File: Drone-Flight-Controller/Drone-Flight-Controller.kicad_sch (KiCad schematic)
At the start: 45 parts, among them J1 Screw_Terminal_01x02, J10 TestPoint, J11 TestPoint, J12 TestPoint, J2 Raspberry_Pi_4, J3 TestPoint, J4 TestPoint, J5 TestPoint, J6 TestPoint, J7 TestPoint, J8 TestPoint, J9 TestPoint, SW1 SW_Omron_B3FS, U1 LMR51430, U2 ADC101C021CIMK, U3 MPU-9150, U4 BMP280, U5 PCA9531PW

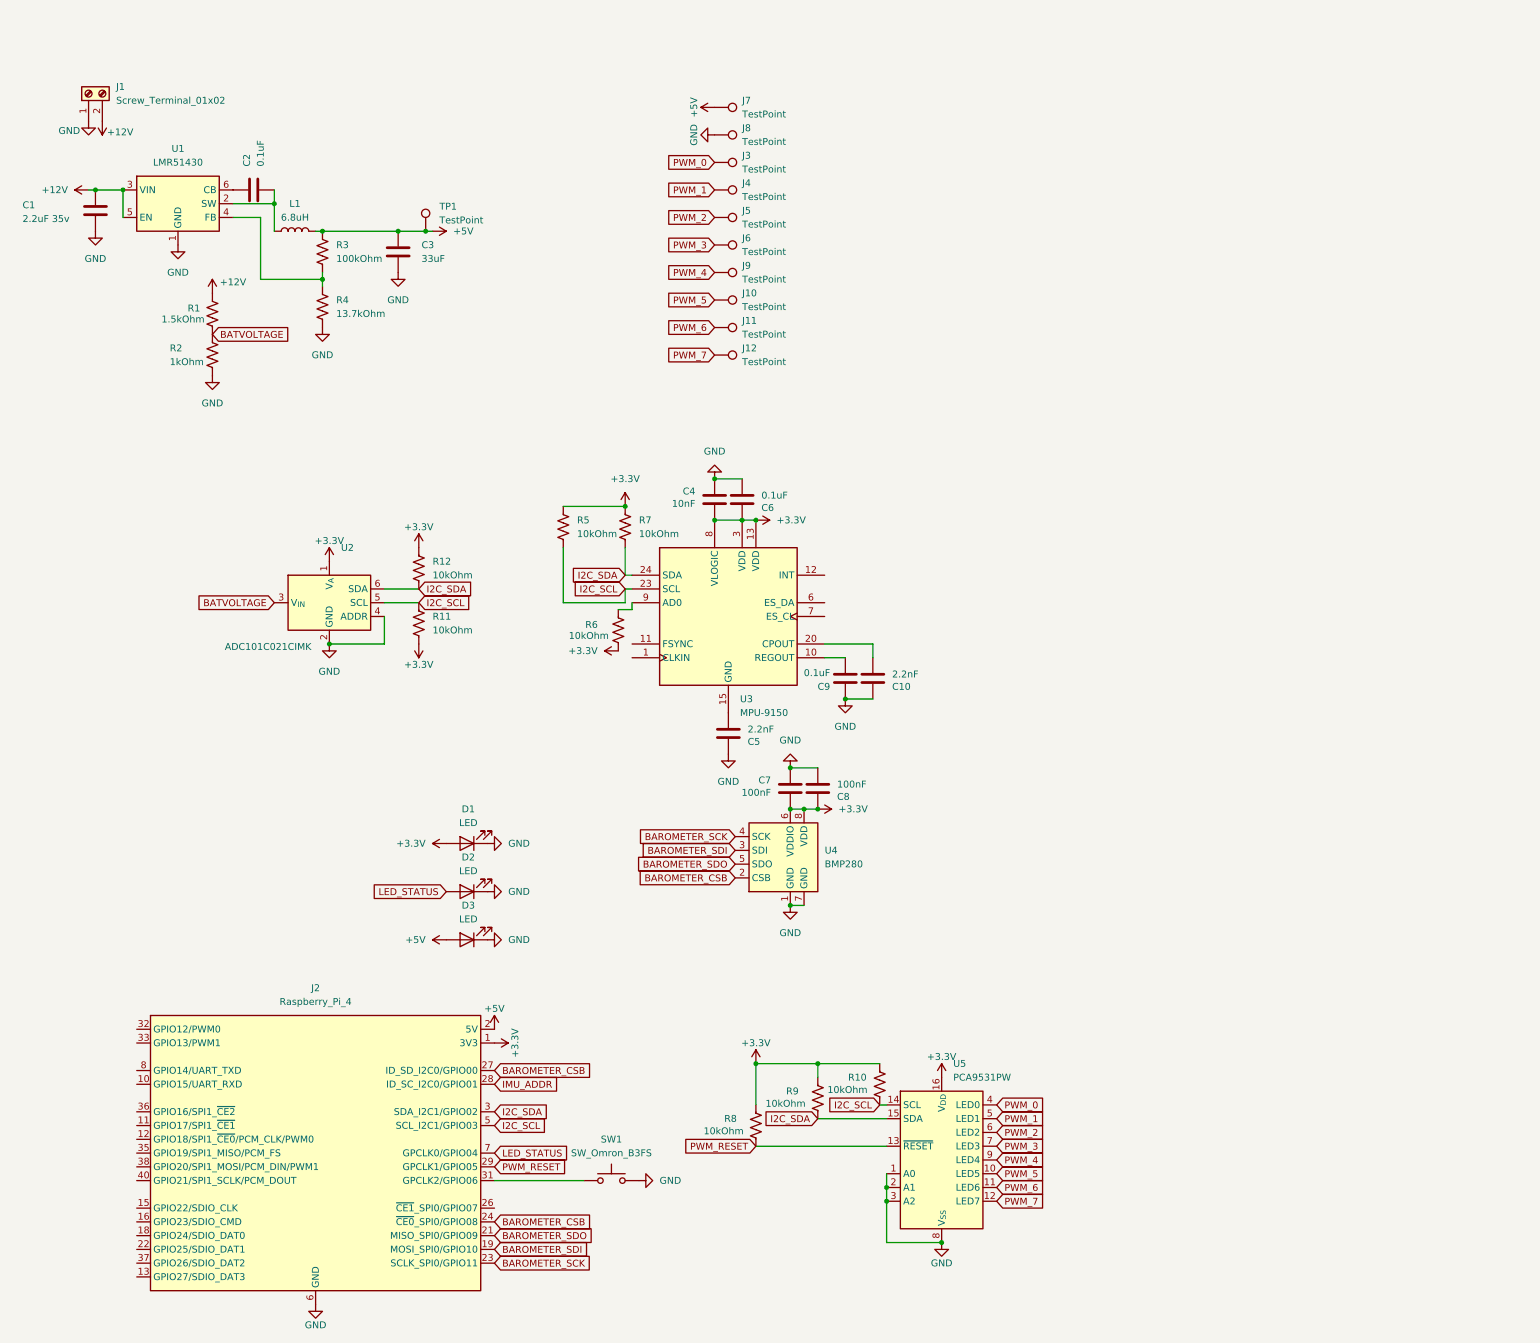
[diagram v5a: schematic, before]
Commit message: add a fuse
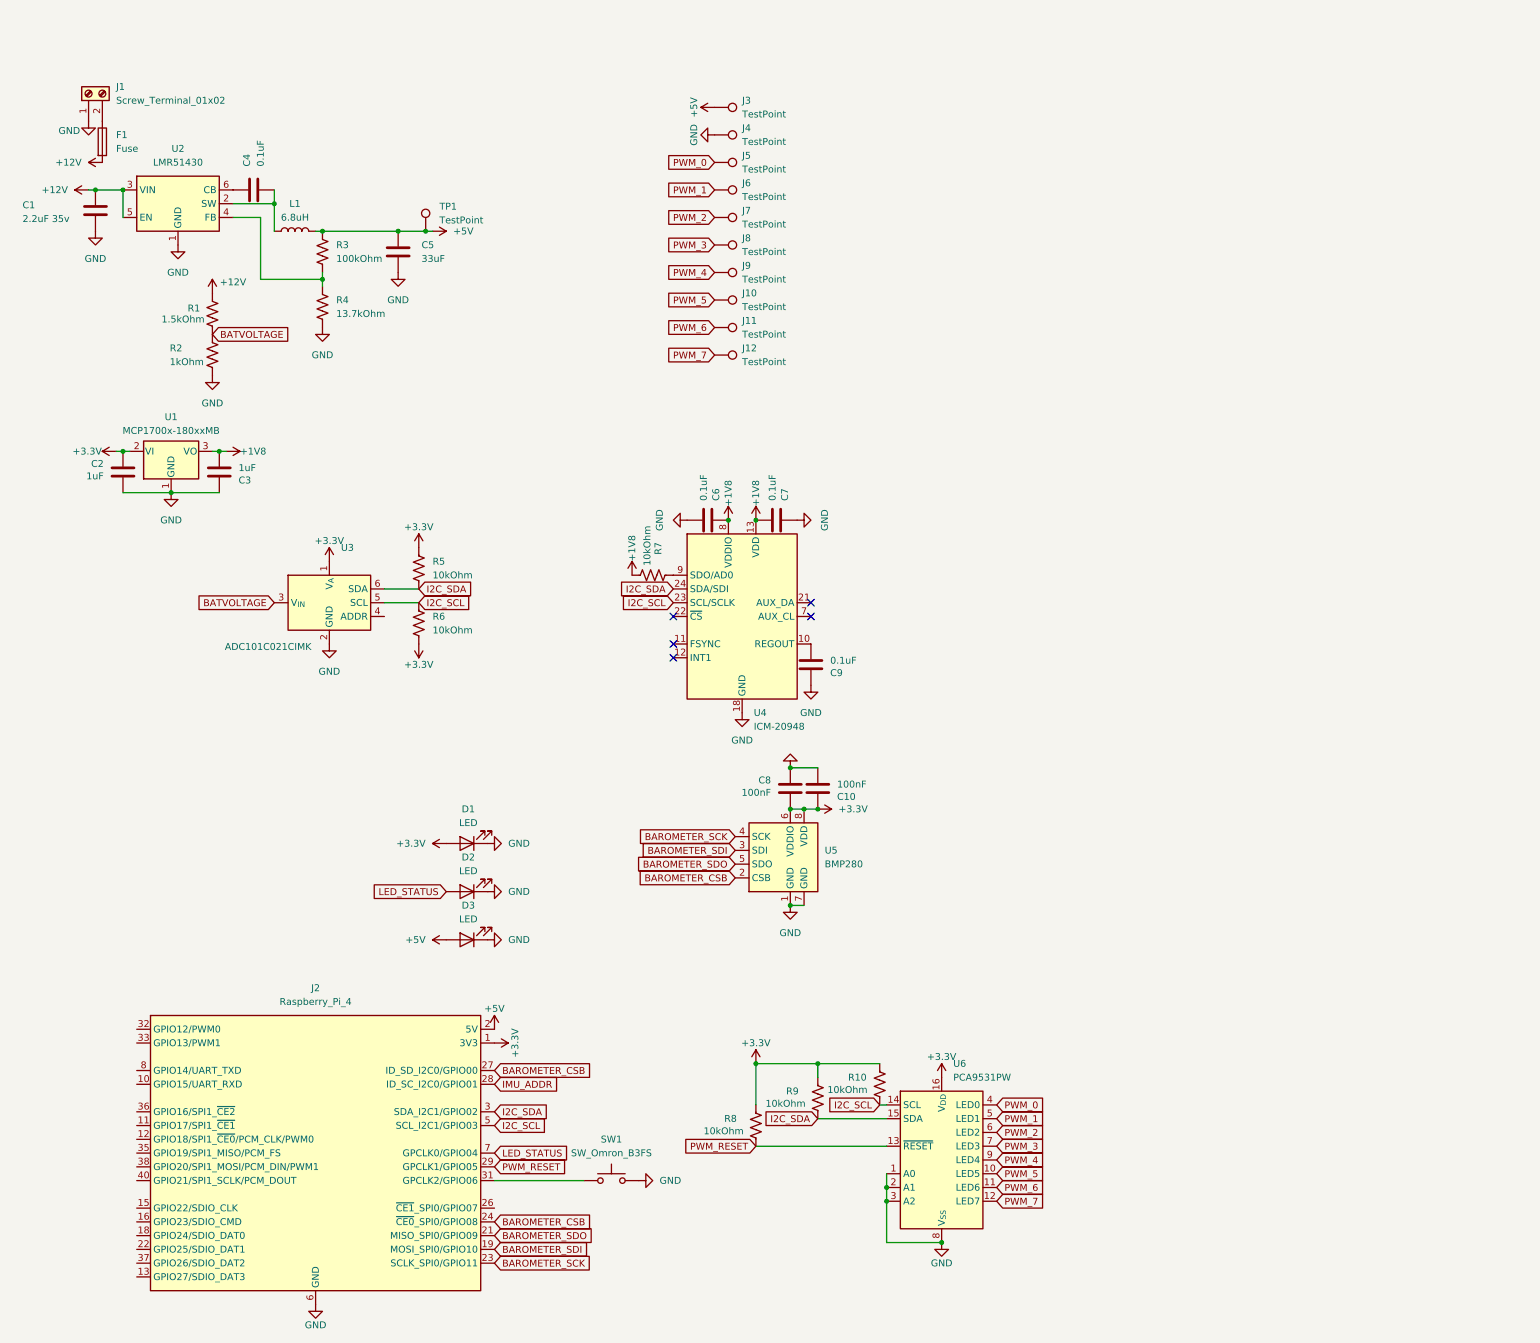
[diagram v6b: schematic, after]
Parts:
- removed C10, C5: 2.2nF, Capacitor_SMD:C_0402_1005Metric, symbol Device:C
- removed C4: 10nF, Capacitor_SMD:C_0402_1005Metric, symbol Device:C
- removed R5, R6: 10kOhm, Resistor_SMD:R_0402_1005Metric, symbol Device:R_US
- removed U3: MPU-9150, Sensor_Motion:InvenSense_QFN-24_4x4mm_P0.5mm, symbol Sensor_Motion:MPU-9150
- added C2, C3: 1uF, Capacitor_SMD:C_0402_1005Metric, symbol Device:C
- added C7: 0.1uF, Capacitor_SMD:C_0402_1005Metric, symbol Device:C
- added F1: Fuse, Fuse:Fuse_1206_3216Metric, symbol Device:Fuse
- added U1: MCP1700x-180xxMB, Package_TO_SOT_SMD:SOT-89-3, symbol Regulator_Linear:MCP1700x-180xxMB
- added U4: ICM-20948, Sensor_Motion:InvenSense_QFN-24_3x3mm_P0.4mm, symbol Sensor_Motion:ICM-20948
- renumbered C8 to C10, C2 to C4, C3 to C5, C7 to C8, J7 to J3, J8 to J4, J3 to J5, J4 to J6, J5 to J7, J6 to J8, R12 to R5, R11 to R6, U1 to U2, U2 to U3, U4 to U5, U5 to U6
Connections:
- net +12V: now also F1.2; no longer J1.2 (Pin_2)
- net +3.3V: now also C2.2, U1.2 (VI); no longer C6.2, R7.1
- net GND: now also C9.2, C2.1, C3.2, C7.2, U1.1 (GND), U4.18 (GND), U4.20 (GND); no longer C9.1, U3.4 (ADDR)
- net I2C_SCL: now also U4.23 (SCL/SCLK)
- net I2C_SDA: now also U4.24 (SDA/SDI); no longer R7.2
- new net: C9.1, U4.10 (REGOUT)
- new net: R7.1, U4.9 (SDO/AD0)
- new net: F1.1, J1.2 (Pin_2)
- new net +1V8: C3.1, C6.2, C7.1, R7.2, U1.3 (VO), U4.13 (VDD), U4.8 (VDDIO)
- no-connect marks 0 -> 5

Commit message: added imu level shifter
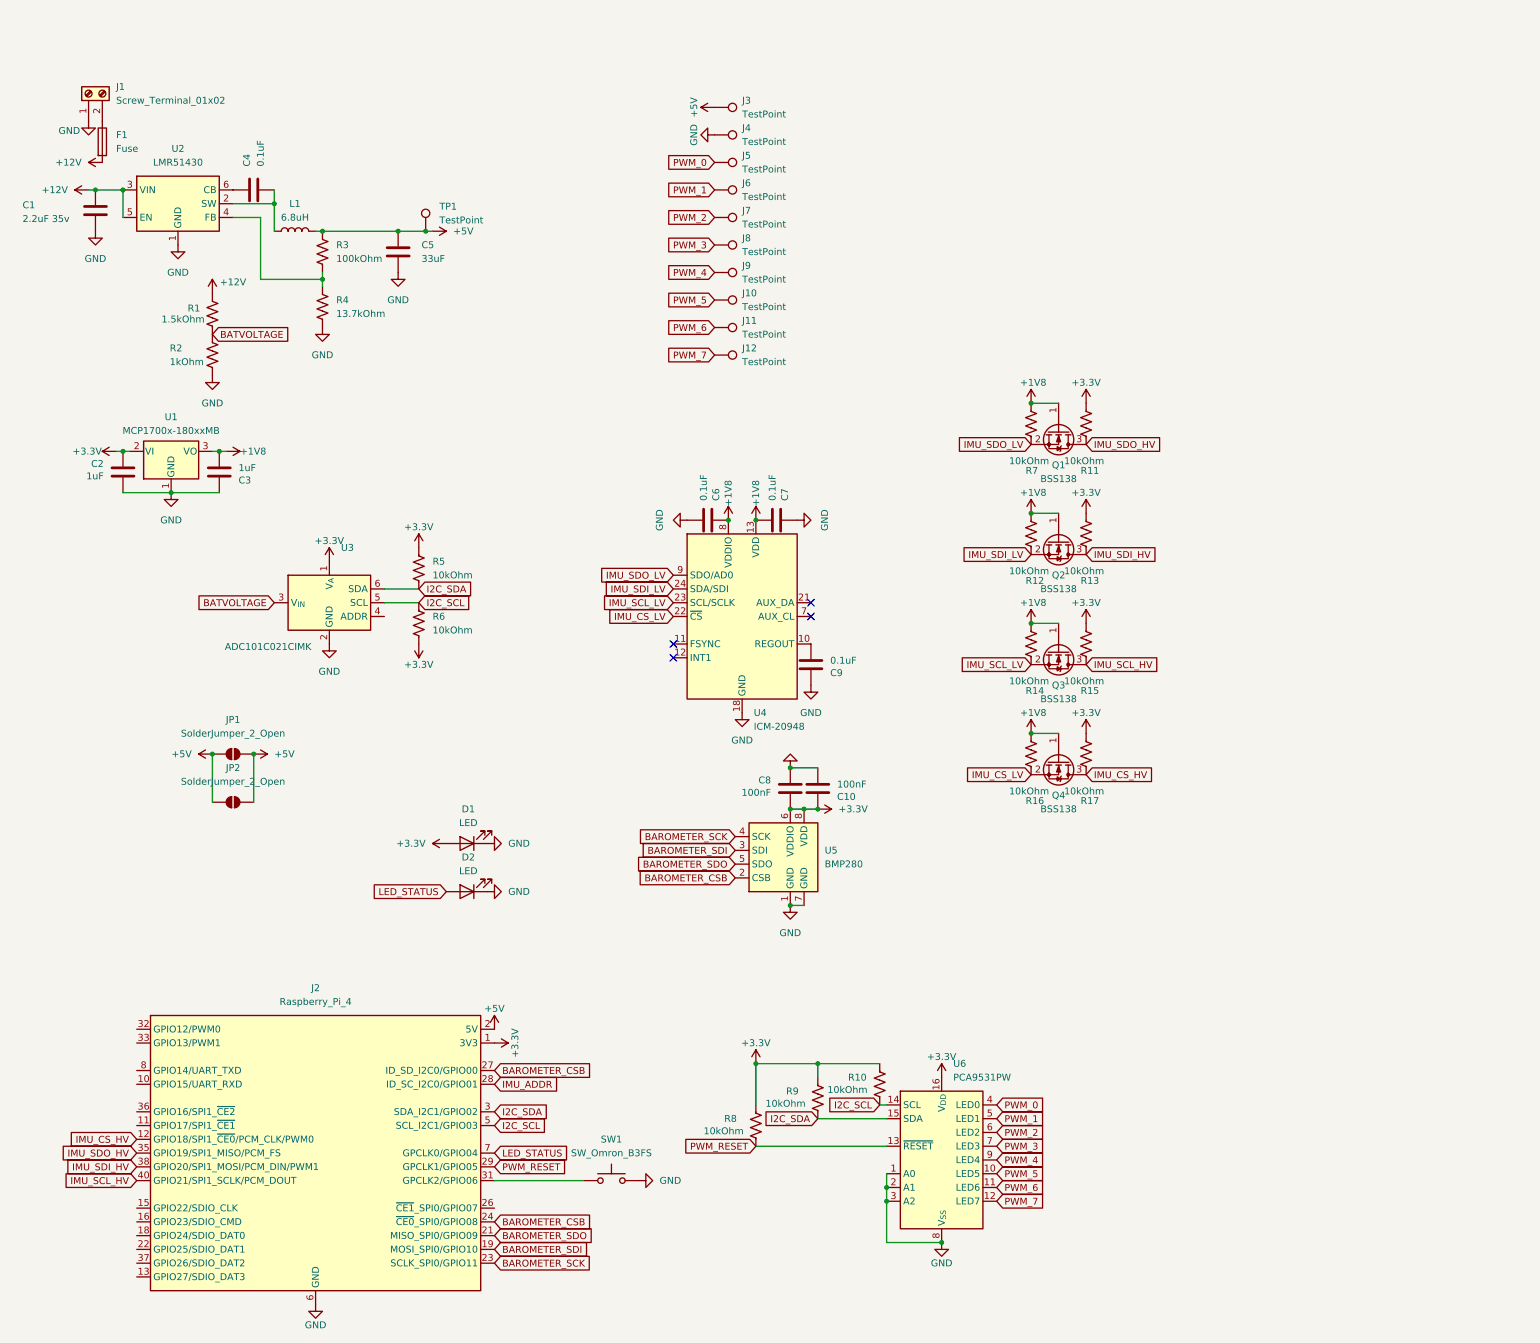
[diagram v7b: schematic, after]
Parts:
- removed D3: LED, LED_SMD:LED_0402_1005Metric, symbol Device:LED
- added JP1, JP2: SolderJumper_2_Open, Jumper:SolderJumper-2_P1.3mm_Open_Pad1.0x1.5mm, symbol Jumper:SolderJumper_2_Open
- added Q1, Q2, Q3, Q4: BSS138, Package_TO_SOT_SMD:SOT-23, symbol Transistor_FET:BSS138
- added R11, R12, R13, R14, R15, R16, R17: 10kOhm, Resistor_SMD:R_0402_1005Metric, symbol Device:R_US
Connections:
- net +1V8: now also Q1.1 (G), Q2.1 (G), Q3.1 (G), Q4.1 (G), R12.2, R14.2, R16.2
- net +3.3V: now also R11.2, R13.2, R15.2, R17.2
- net +5V: now also JP1.1 (A), JP1.2 (B), JP2.1 (A), JP2.2 (B)
- net I2C_SCL: no longer U4.23 (SCL/SCLK)
- net I2C_SDA: no longer U4.24 (SDA/SDI)
- net IMU_CS_LV: now reaches U4.22 (~{CS})
- net IMU_CS_LV: now also Q4.2 (S), R16.1
- net IMU_SDO_LV: now reaches R7.1, U4.9 (SDO/AD0)
- net IMU_SDO_LV: now also Q1.2 (S)
- net IMU_CS_HV: now reaches J2.12 (GPIO18/SPI1_~{CE0}/PCM_CLK/PWM0)
- net IMU_CS_HV: now also Q4.3 (D), R17.1
- net IMU_SDO_HV: now reaches J2.35 (GPIO19/SPI1_MISO/PCM_FS)
- net IMU_SDO_HV: now also Q1.3 (D), R11.1
- net IMU_SDI_HV: now reaches J2.38 (GPIO20/SPI1_MOSI/PCM_DIN/PWM1)
- net IMU_SDI_HV: now also Q2.3 (D), R13.1
- net IMU_SCL_HV: now reaches J2.40 (GPIO21/SPI1_SCLK/PCM_DOUT)
- net IMU_SCL_HV: now also Q3.3 (D), R15.1
- new net IMU_SCL_LV: Q3.2 (S), R14.1, U4.23 (SCL/SCLK)
- new net IMU_SDI_LV: Q2.2 (S), R12.1, U4.24 (SDA/SDI)
- no-connect marks 5 -> 4
